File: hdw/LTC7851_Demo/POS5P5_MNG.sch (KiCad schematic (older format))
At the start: 8 parts

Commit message: Added component values for all phase 1 components
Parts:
- removed C?: 100uF, symbol LED_Display_Local_Library:CP_Tant_Custom
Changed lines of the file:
@@
 $Descr A 11000 8500
 encoding utf-8
-Sheet 8 15
+Sheet 8 14
 Title ""
 Date ""
@@
 Comment4 ""
 $EndDescr
-$Comp
-L LED_Display_Local_Library:CP_Tant_Custom C?
-U 1 1 5BBB1259
-P 7040 3820
-AR Path="/5BB86F23/5BBB1259" Ref="C?"  Part="1"
-AR Path="/5BB9CE4B/5BBB1259" Ref="C?"  Part="1"
-F 0 "C?" H 7065 3920 50  0000 L CNN
-F 1 "100uF" H 7065 3720 50  0000 L CNN
-F 2 "" H 7078 3670 50  0001 C CNN
-F 3 "" H 7065 3920 50  0001 C CNN
-F 4 "718-1102-1-ND" H 7040 3820 50  0001 C CNN "Digi-Key PN"
-F 5 "7343" H 6890 3920 50  0000 R CNN "display_footprint"
-F 6 "16V" H 6890 3820 50  0000 R CNN "Voltage"
-F 7 "10%" H 6890 3720 50  0000 R CNN "Tolerance"
-	1    7040 3820
-	1    0    0    -1
-$EndComp
 Wire Wire Line
 	3800 3510 3800 3590

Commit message: Duplicated master phase, added status LEDs and a few test points
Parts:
- removed C?: C, symbol Custom_Library:C_Custom
- removed C?: 10uF, symbol Custom_Library:C_Custom
- removed R?: R, symbol Custom_Library:R_Custom
- added C?: 100uF, symbol Custom_Library:CP_Tant_Custom
- added C?: 0.1uF, symbol Custom_Library:C_Custom
- added C?: 10uF, symbol Custom_Library:CP_Tant_Custom
- added R?: 680, symbol Custom_Library:R_Custom
- R?: value R -> 200; Tolerance Tol -> 1%; Wattage W -> 1/10W; display_footprint Foot -> 0603
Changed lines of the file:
@@
-$Comp
-L Custom_Library:C_Custom C?
-U 1 1 5BBB0B35
-P 3800 3820
-F 0 "C?" H 3825 3920 50  0000 L CNN
-F 1 "10uF" H 3825 3720 50  0000 L CNN
-F 2 "" H 3838 3670 50  0001 C CNN
-F 3 "" H 3825 3920 50  0001 C CNN
-F 4 "Foot" H 3650 3920 50  0000 R CNN "display_footprint"
-F 5 "V" H 3650 3820 50  0000 R CNN "Voltage"
-F 6 "Er" H 3650 3720 50  0000 R CNN "Dielectric"
-F 7 "PN" H 4225 4320 60  0001 C CNN "Digi-Key PN"
-	1    3800 3820
-	1    0    0    -1
-$EndComp
 $Comp
 L Custom_Library:C_Custom C?
@@
 $EndComp
 $Comp
-L Custom_Library:C_Custom C?
-U 1 1 5BBB004E
-P 5130 4280
-F 0 "C?" H 5155 4380 50  0000 L CNN
-F 1 "C" H 5155 4180 50  0000 L CNN
-F 2 "" H 5168 4130 50  0001 C CNN
-F 3 "" H 5155 4380 50  0001 C CNN
-F 4 "Foot" H 4980 4380 50  0000 R CNN "display_footprint"
-F 5 "V" H 4980 4280 50  0000 R CNN "Voltage"
-F 6 "Er" H 4980 4180 50  0000 R CNN "Dielectric"
-F 7 "PN" H 5555 4780 60  0001 C CNN "Digi-Key PN"
-	1    5130 4280
-	1    0    0    -1
-$EndComp
-$Comp
 L power:GND #PWR?
 U 1 1 5BBAFFEC
@@
 $Comp
 L Custom_Library:R_Custom R?
-U 1 1 5BBAFF2B
-P 5770 4280
-AR Path="/5BB86F29/5BBAFF2B" Ref="R?"  Part="1"
-AR Path="/5BB9CE4B/5BBAFF2B" Ref="R?"  Part="1"
-F 0 "R?" H 5670 4280 50  0000 R CNN
-F 1 "R" V 5770 4280 50  0000 C CNN
-F 2 "" H 5770 4280 50  0001 C CNN
-F 3 "" H 5770 4280 50  0001 C CNN
-F 4 "PN" H 6070 4680 60  0001 C CNN "Digi-Key PN"
-F 5 "Foot" H 5870 4360 50  0000 L CNN "display_footprint"
-F 6 "Tol" H 5870 4280 50  0000 L CNN "Tolerance"
-F 7 "W" H 5870 4200 50  0000 L CNN "Wattage"
-	1    5770 4280
-	-1   0    0    -1
-$EndComp
-$Comp
-L Custom_Library:R_Custom R?
 U 1 1 5BBAFF04
 P 5770 3820
@@
 AR Path="/5BB9CE4B/5BBAFF04" Ref="R?"  Part="1"
 F 0 "R?" H 5670 3820 50  0000 R CNN
-F 1 "R" V 5770 3820 50  0000 C CNN
+F 1 "200" V 5770 3820 50  0000 C CNN
 F 2 "" H 5770 3820 50  0001 C CNN
 F 3 "" H 5770 3820 50  0001 C CNN
 F 4 "PN" H 6070 4220 60  0001 C CNN "Digi-Key PN"
-F 5 "Foot" H 5870 3900 50  0000 L CNN "display_footprint"
-F 6 "Tol" H 5870 3820 50  0000 L CNN "Tolerance"
-F 7 "W" H 5870 3740 50  0000 L CNN "Wattage"
+F 5 "0603" H 5870 3900 50  0000 L CNN "display_footprint"
+F 6 "1%" H 5870 3820 50  0000 L CNN "Tolerance"
+F 7 "1/10W" H 5870 3740 50  0000 L CNN "Wattage"
 	1    5770 3820
 	-1   0    0    -1
@@
 	1    0    0    -1
 $EndComp
+$Comp
+L Custom_Library:CP_Tant_Custom C?
+U 1 1 5BD4FFF4
+P 7040 3820
+AR Path="/5BB86F29/5BD4FFF4" Ref="C?"  Part="1"
+AR Path="/5BB86F2C/5BD4FFF4" Ref="C?"  Part="1"
+AR Path="/5BB86F2F/5BD4FFF4" Ref="C?"  Part="1"
+AR Path="/5BB9CE4B/5BD4FFF4" Ref="C?"  Part="1"
+F 0 "C?" H 7065 3920 50  0000 L CNN
+F 1 "100uF" H 7065 3720 50  0000 L CNN
+F 2 "" H 7078 3670 50  0001 C CNN
+F 3 "" H 7065 3920 50  0001 C CNN
+F 4 "478-9994-1-ND" H 7040 3820 50  0001 C CNN "Digi-Key PN"
+F 5 "3528" H 6890 3920 50  0000 R CNN "display_footprint"
+F 6 "6.3V" H 6890 3820 50  0000 R CNN "Voltage"
+F 7 "20%" H 6890 3720 50  0000 R CNN "Tolerance"
+	1    7040 3820
+	1    0    0    -1
+$EndComp
+$Comp
+L Custom_Library:R_Custom R?
+U 1 1 5BD50813
+P 5770 4280
+AR Path="/5BB86F29/5BD50813" Ref="R?"  Part="1"
+AR Path="/5BB9CE4B/5BD50813" Ref="R?"  Part="1"
+F 0 "R?" H 5670 4280 50  0000 R CNN
+F 1 "680" V 5770 4280 50  0000 C CNN
+F 2 "" H 5770 4280 50  0001 C CNN
+F 3 "" H 5770 4280 50  0001 C CNN
+F 4 "PN" H 6070 4680 60  0001 C CNN "Digi-Key PN"
+F 5 "0603" H 5870 4360 50  0000 L CNN "display_footprint"
+F 6 "1%" H 5870 4280 50  0000 L CNN "Tolerance"
+F 7 "1/10W" H 5870 4200 50  0000 L CNN "Wattage"
+	1    5770 4280
+	-1   0    0    -1
+$EndComp
+$Comp
+L Custom_Library:C_Custom C?
+U 1 1 5BD51214
+P 5130 4280
+F 0 "C?" H 5155 4380 50  0000 L CNN
+F 1 "0.1uF" H 5155 4180 50  0000 L CNN
+F 2 "" H 5168 4130 50  0001 C CNN
+F 3 "" H 5155 4380 50  0001 C CNN
+F 4 "0603" H 4980 4380 50  0000 R CNN "display_footprint"
+F 5 "50V" H 4980 4280 50  0000 R CNN "Voltage"
+F 6 "X7R" H 4980 4180 50  0000 R CNN "Dielectric"
+F 7 "PN" H 5555 4780 60  0001 C CNN "Digi-Key PN"
+	1    5130 4280
+	1    0    0    -1
+$EndComp
+$Comp
+L Custom_Library:CP_Tant_Custom C?
+U 1 1 5BD5196E
+P 3800 3820
+AR Path="/5BB86F29/5BD5196E" Ref="C?"  Part="1"
+AR Path="/5BB86F2C/5BD5196E" Ref="C?"  Part="1"
+AR Path="/5BB86F2F/5BD5196E" Ref="C?"  Part="1"
+AR Path="/5BB9CE4B/5BD5196E" Ref="C?"  Part="1"
+F 0 "C?" H 3825 3920 50  0000 L CNN
+F 1 "10uF" H 3825 3720 50  0000 L CNN
+F 2 "" H 3838 3670 50  0001 C CNN
+F 3 "" H 3825 3920 50  0001 C CNN
+F 4 "399-5034-1-ND" H 3800 3820 50  0001 C CNN "Digi-Key PN"
+F 5 "3528" H 3650 3920 50  0000 R CNN "display_footprint"
+F 6 "16V" H 3650 3820 50  0000 R CNN "Voltage"
+F 7 "10%" H 3650 3720 50  0000 R CNN "Tolerance"
+	1    3800 3820
+	1    0    0    -1
+$EndComp

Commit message: Annotated schematic
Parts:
- added TP801: TP, symbol Custom_Library:TP
- gave numbers to parts that had none: 8
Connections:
- wire segments 17 -> 19
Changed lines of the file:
@@
 	3800 3510 3800 3590
 $Comp
-L power:+12V #PWR?
+L power:+12V #PWR0801
 U 1 1 5BBB0D98
 P 3800 3510
-F 0 "#PWR?" H 3800 3360 50  0001 C CNN
+F 0 "#PWR0801" H 3800 3360 50  0001 C CNN
 F 1 "+12V" H 3800 3650 50  0000 C CNN
 F 2 "" H 3800 3510 50  0001 C CNN
@@
 	3800 3670 3800 3590
 $Comp
-L power:GND #PWR?
+L power:GND #PWR0802
 U 1 1 5BBB0B8E
 P 3800 3970
-F 0 "#PWR?" H 3800 3720 50  0001 C CNN
+F 0 "#PWR0802" H 3800 3720 50  0001 C CNN
 F 1 "GND" H 3800 3820 50  0000 C CNN
 F 2 "" H 3800 3970 50  0001 C CNN
@@
 $EndComp
 $Comp
-L power:GND #PWR?
+L power:GND #PWR0803
 U 1 1 5BBB0B63
 P 4460 3970
-F 0 "#PWR?" H 4460 3720 50  0001 C CNN
+F 0 "#PWR0803" H 4460 3720 50  0001 C CNN
 F 1 "GND" H 4460 3820 50  0000 C CNN
 F 2 "" H 4460 3970 50  0001 C CNN
@@
 $EndComp
 $Comp
-L Custom_Library:C_Custom C?
+L Custom_Library:C_Custom C802
 U 1 1 5BBB0AFB
 P 4460 3820
-F 0 "C?" H 4485 3920 50  0000 L CNN
+F 0 "C802" H 4485 3920 50  0000 L CNN
 F 1 "0.1uF" H 4485 3720 50  0000 L CNN
 F 2 "" H 4498 3670 50  0001 C CNN
@@
 	7040 3510 7040 3590
 $Comp
-L Custom_Library:+5.5V_MNG #PWR?
+L Custom_Library:+5.5V_MNG #PWR0807
 U 1 1 5BBB0807
 P 7040 3510
-F 0 "#PWR?" H 7040 3360 50  0001 C CNN
+F 0 "#PWR0807" H 7040 3360 50  0001 C CNN
 F 1 "+5.5V_MNG" H 7040 3650 50  0000 C CNN
 F 2 "" H 7040 3510 50  0001 C CNN
@@
 	7040 3670 7040 3590
 $Comp
-L power:GND #PWR?
+L power:GND #PWR0808
 U 1 1 5BBB04B3
 P 7040 3970
-F 0 "#PWR?" H 7040 3720 50  0001 C CNN
+F 0 "#PWR0808" H 7040 3720 50  0001 C CNN
 F 1 "GND" H 7040 3820 50  0000 C CNN
 F 2 "" H 7040 3970 50  0001 C CNN
@@
 	6430 3670 6430 3590
 $Comp
-L power:GND #PWR?
+L power:GND #PWR0806
 U 1 1 5BBB0393
 P 6430 3970
-F 0 "#PWR?" H 6430 3720 50  0001 C CNN
+F 0 "#PWR0806" H 6430 3720 50  0001 C CNN
 F 1 "GND" H 6430 3820 50  0000 C CNN
 F 2 "" H 6430 3970 50  0001 C CNN
@@
 $EndComp
 $Comp
-L Custom_Library:C_Custom C?
+L Custom_Library:C_Custom C804
 U 1 1 5BBB0328
 P 6430 3820
-F 0 "C?" H 6455 3920 50  0000 L CNN
+F 0 "C804" H 6455 3920 50  0000 L CNN
 F 1 "0.1uF" H 6455 3720 50  0000 L CNN
 F 2 "" H 6468 3670 50  0001 C CNN
@@
 	5130 4130 5130 4040
 $Comp
-L power:GND #PWR?
+L power:GND #PWR0804
 U 1 1 5BBB0089
 P 5130 4430
-F 0 "#PWR?" H 5130 4180 50  0001 C CNN
+F 0 "#PWR0804" H 5130 4180 50  0001 C CNN
 F 1 "GND" H 5130 4280 50  0000 C CNN
 F 2 "" H 5130 4430 50  0001 C CNN
@@
 $EndComp
 $Comp
-L power:GND #PWR?
+L power:GND #PWR0805
 U 1 1 5BBAFFEC
 P 5770 4430
-F 0 "#PWR?" H 5770 4180 50  0001 C CNN
+F 0 "#PWR0805" H 5770 4180 50  0001 C CNN
 F 1 "GND" H 5770 4280 50  0000 C CNN
 F 2 "" H 5770 4430 50  0001 C CNN
@@
 P 5770 3820
 AR Path="/5BB86F29/5BBAFF04" Ref="R?"  Part="1"
-AR Path="/5BB9CE4B/5BBAFF04" Ref="R?"  Part="1"
-F 0 "R?" H 5670 3820 50  0000 R CNN
+AR Path="/5BB9CE4B/5BBAFF04" Ref="R801"  Part="1"
+F 0 "R801" H 5670 3820 50  0000 R CNN
 F 1 "200" V 5770 3820 50  0000 C CNN
 F 2 "" H 5770 3820 50  0001 C CNN
@@
 $EndComp
 $Comp
-L Regulator_Linear:LM1117-ADJ U?
+L Regulator_Linear:LM1117-ADJ U801
 U 1 1 5BBA7A89
 P 5130 3590
-F 0 "U?" H 4980 3715 50  0000 C CNN
+F 0 "U801" H 4980 3715 50  0000 C CNN
 F 1 "LM1117-ADJ" H 5130 3715 50  0000 L CNN
 F 2 "" H 5130 3590 50  0001 C CNN
@@
 AR Path="/5BB86F2C/5BD4FFF4" Ref="C?"  Part="1"
 AR Path="/5BB86F2F/5BD4FFF4" Ref="C?"  Part="1"
-AR Path="/5BB9CE4B/5BD4FFF4" Ref="C?"  Part="1"
-F 0 "C?" H 7065 3920 50  0000 L CNN
+AR Path="/5BB9CE4B/5BD4FFF4" Ref="C805"  Part="1"
+F 0 "C805" H 7065 3920 50  0000 L CNN
 F 1 "100uF" H 7065 3720 50  0000 L CNN
 F 2 "" H 7078 3670 50  0001 C CNN
@@
 P 5770 4280
 AR Path="/5BB86F29/5BD50813" Ref="R?"  Part="1"
-AR Path="/5BB9CE4B/5BD50813" Ref="R?"  Part="1"
-F 0 "R?" H 5670 4280 50  0000 R CNN
+AR Path="/5BB9CE4B/5BD50813" Ref="R802"  Part="1"
+F 0 "R802" H 5670 4280 50  0000 R CNN
 F 1 "680" V 5770 4280 50  0000 C CNN
 F 2 "" H 5770 4280 50  0001 C CNN
@@
 $EndComp
 $Comp
-L Custom_Library:C_Custom C?
+L Custom_Library:C_Custom C803
 U 1 1 5BD51214
 P 5130 4280
-F 0 "C?" H 5155 4380 50  0000 L CNN
+F 0 "C803" H 5155 4380 50  0000 L CNN
 F 1 "0.1uF" H 5155 4180 50  0000 L CNN
 F 2 "" H 5168 4130 50  0001 C CNN
@@
 AR Path="/5BB86F2C/5BD5196E" Ref="C?"  Part="1"
 AR Path="/5BB86F2F/5BD5196E" Ref="C?"  Part="1"
-AR Path="/5BB9CE4B/5BD5196E" Ref="C?"  Part="1"
-F 0 "C?" H 3825 3920 50  0000 L CNN
+AR Path="/5BB9CE4B/5BD5196E" Ref="C801"  Part="1"
+F 0 "C801" H 3825 3920 50  0000 L CNN
 F 1 "10uF" H 3825 3720 50  0000 L CNN
 F 2 "" H 3838 3670 50  0001 C CNN
@@
 	1    0    0    -1
 $EndComp
+$Comp
+L power:PWR_FLAG #FLG0801
+U 1 1 5BC40B21
+P 5770 3510
+F 0 "#FLG0801" H 5770 3585 50  0001 C CNN
+F 1 "PWR_FLAG" H 5770 3660 50  0000 C CNN
+F 2 "" H 5770 3510 50  0001 C CNN
+F 3 "~" H 5770 3510 50  0001 C CNN
+	1    5770 3510
+	1    0    0    -1
+$EndComp
+Wire Wire Line
+	5770 3510 5770 3590
+$Comp
+L Custom_Library:TP TP801
+U 1 1 5BC40C98
+P 6430 3510
+F 0 "TP801" H 6430 3660 50  0000 C CNN
+F 1 "TP" H 6430 3660 50  0001 C CNN
+F 2 "" H 6430 3510 60  0000 C CNN
+F 3 "" H 6430 3510 60  0000 C CNN
+	1    6430 3510
+	1    0    0    -1
+$EndComp
+Wire Wire Line
+	6430 3510 6430 3590
 $EndSCHEMATC

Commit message: Cleaned up for ERC
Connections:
- wire segments 19 -> 18
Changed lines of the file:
@@
 $EndComp
-$Comp
-L power:PWR_FLAG #FLG0801
-U 1 1 5BC40B21
-P 5770 3510
-F 0 "#FLG0801" H 5770 3585 50  0001 C CNN
-F 1 "PWR_FLAG" H 5770 3660 50  0000 C CNN
-F 2 "" H 5770 3510 50  0001 C CNN
-F 3 "~" H 5770 3510 50  0001 C CNN
-	1    5770 3510
-	1    0    0    -1
-$EndComp
-Wire Wire Line
-	5770 3510 5770 3590
 $Comp
 L Custom_Library:TP TP801

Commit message: Added Digi-Key part numbers for all parts
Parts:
- C802, C803, C804: Digi-Key PN PN -> 490-4779-1-ND
- R801: Digi-Key PN PN -> MCT0603-200-CFCT-ND
- R802: Digi-Key PN PN -> P680HCT-ND
- U801: Digi-Key PN (none) -> LM1117IMPX-ADJ/NOPBCT-ND
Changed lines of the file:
@@
 F 5 "50V" H 4310 3820 50  0000 R CNN "Voltage"
 F 6 "X7R" H 4310 3720 50  0000 R CNN "Dielectric"
-F 7 "PN" H 4885 4320 60  0001 C CNN "Digi-Key PN"
+F 7 "490-4779-1-ND" H 4885 4320 60  0001 C CNN "Digi-Key PN"
 	1    4460 3820
 	1    0    0    -1
@@
 F 5 "50V" H 6280 3820 50  0000 R CNN "Voltage"
 F 6 "X7R" H 6280 3720 50  0000 R CNN "Dielectric"
-F 7 "PN" H 6855 4320 60  0001 C CNN "Digi-Key PN"
+F 7 "490-4779-1-ND" H 6855 4320 60  0001 C CNN "Digi-Key PN"
 	1    6430 3820
 	1    0    0    -1
@@
 F 2 "" H 5770 3820 50  0001 C CNN
 F 3 "" H 5770 3820 50  0001 C CNN
-F 4 "PN" H 6070 4220 60  0001 C CNN "Digi-Key PN"
+F 4 "MCT0603-200-CFCT-ND" H 6070 4220 60  0001 C CNN "Digi-Key PN"
 F 5 "0603" H 5870 3900 50  0000 L CNN "display_footprint"
 F 6 "1%" H 5870 3820 50  0000 L CNN "Tolerance"
@@
 F 2 "" H 5130 3590 50  0001 C CNN
 F 3 "http://www.ti.com/lit/ds/symlink/lm1117.pdf" H 5130 3590 50  0001 C CNN
+F 4 "LM1117IMPX-ADJ/NOPBCT-ND" H 0   0   50  0001 C CNN "Digi-Key PN"
 	1    5130 3590
 	1    0    0    -1
@@
 F 2 "" H 5770 4280 50  0001 C CNN
 F 3 "" H 5770 4280 50  0001 C CNN
-F 4 "PN" H 6070 4680 60  0001 C CNN "Digi-Key PN"
+F 4 "P680HCT-ND" H 6070 4680 60  0001 C CNN "Digi-Key PN"
 F 5 "0603" H 5870 4360 50  0000 L CNN "display_footprint"
 F 6 "1%" H 5870 4280 50  0000 L CNN "Tolerance"
@@
 F 5 "50V" H 4980 4280 50  0000 R CNN "Voltage"
 F 6 "X7R" H 4980 4180 50  0000 R CNN "Dielectric"
-F 7 "PN" H 5555 4780 60  0001 C CNN "Digi-Key PN"
+F 7 "490-4779-1-ND" H 5555 4780 60  0001 C CNN "Digi-Key PN"
 	1    5130 4280
 	1    0    0    -1

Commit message: Assigned footprints
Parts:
- C801, C805: footprint (none) -> Capacitors_Tantalum_SMD:CP_Tantalum_Case-B_EIA-3528-21_Reflow
- C802, C803, C804: footprint (none) -> Capacitors_SMD:C_0603
- R801, R802: footprint (none) -> Resistors_SMD:R_0603
- TP801: footprint (none) -> Measurement_Points:Measurement_Point_Round-SMD-Pad_Small
- U801: footprint (none) -> TO_SOT_Packages_SMD:SOT-223-3_TabPin2
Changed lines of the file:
@@
 F 0 "C802" H 4485 3920 50  0000 L CNN
 F 1 "0.1uF" H 4485 3720 50  0000 L CNN
-F 2 "" H 4498 3670 50  0001 C CNN
+F 2 "Capacitors_SMD:C_0603" H 4498 3670 50  0001 C CNN
 F 3 "" H 4485 3920 50  0001 C CNN
 F 4 "0603" H 4310 3920 50  0000 R CNN "display_footprint"
@@
 F 0 "C804" H 6455 3920 50  0000 L CNN
 F 1 "0.1uF" H 6455 3720 50  0000 L CNN
-F 2 "" H 6468 3670 50  0001 C CNN
+F 2 "Capacitors_SMD:C_0603" H 6468 3670 50  0001 C CNN
 F 3 "" H 6455 3920 50  0001 C CNN
 F 4 "0603" H 6280 3920 50  0000 R CNN "display_footprint"
@@
 F 0 "R801" H 5670 3820 50  0000 R CNN
 F 1 "200" V 5770 3820 50  0000 C CNN
-F 2 "" H 5770 3820 50  0001 C CNN
+F 2 "Resistors_SMD:R_0603" H 5770 3820 50  0001 C CNN
 F 3 "" H 5770 3820 50  0001 C CNN
 F 4 "MCT0603-200-CFCT-ND" H 6070 4220 60  0001 C CNN "Digi-Key PN"
@@
 F 0 "U801" H 4980 3715 50  0000 C CNN
 F 1 "LM1117-ADJ" H 5130 3715 50  0000 L CNN
-F 2 "" H 5130 3590 50  0001 C CNN
+F 2 "TO_SOT_Packages_SMD:SOT-223-3_TabPin2" H 5130 3590 50  0001 C CNN
 F 3 "http://www.ti.com/lit/ds/symlink/lm1117.pdf" H 5130 3590 50  0001 C CNN
 F 4 "LM1117IMPX-ADJ/NOPBCT-ND" H 0   0   50  0001 C CNN "Digi-Key PN"
@@
 F 0 "C805" H 7065 3920 50  0000 L CNN
 F 1 "100uF" H 7065 3720 50  0000 L CNN
-F 2 "" H 7078 3670 50  0001 C CNN
+F 2 "Capacitors_Tantalum_SMD:CP_Tantalum_Case-B_EIA-3528-21_Reflow" H 7078 3670 50  0001 C CNN
 F 3 "" H 7065 3920 50  0001 C CNN
 F 4 "478-9994-1-ND" H 7040 3820 50  0001 C CNN "Digi-Key PN"
@@
 F 0 "R802" H 5670 4280 50  0000 R CNN
 F 1 "680" V 5770 4280 50  0000 C CNN
-F 2 "" H 5770 4280 50  0001 C CNN
+F 2 "Resistors_SMD:R_0603" H 5770 4280 50  0001 C CNN
 F 3 "" H 5770 4280 50  0001 C CNN
 F 4 "P680HCT-ND" H 6070 4680 60  0001 C CNN "Digi-Key PN"
@@
 F 0 "C803" H 5155 4380 50  0000 L CNN
 F 1 "0.1uF" H 5155 4180 50  0000 L CNN
-F 2 "" H 5168 4130 50  0001 C CNN
+F 2 "Capacitors_SMD:C_0603" H 5168 4130 50  0001 C CNN
 F 3 "" H 5155 4380 50  0001 C CNN
 F 4 "0603" H 4980 4380 50  0000 R CNN "display_footprint"
@@
 F 0 "C801" H 3825 3920 50  0000 L CNN
 F 1 "10uF" H 3825 3720 50  0000 L CNN
-F 2 "" H 3838 3670 50  0001 C CNN
+F 2 "Capacitors_Tantalum_SMD:CP_Tantalum_Case-B_EIA-3528-21_Reflow" H 3838 3670 50  0001 C CNN
 F 3 "" H 3825 3920 50  0001 C CNN
 F 4 "399-5034-1-ND" H 3800 3820 50  0001 C CNN "Digi-Key PN"
@@
 F 0 "TP801" H 6430 3660 50  0000 C CNN
 F 1 "TP" H 6430 3660 50  0001 C CNN
-F 2 "" H 6430 3510 60  0000 C CNN
+F 2 "Measurement_Points:Measurement_Point_Round-SMD-Pad_Small" H 6430 3510 60  0001 C CNN
 F 3 "" H 6430 3510 60  0000 C CNN
 	1    6430 3510

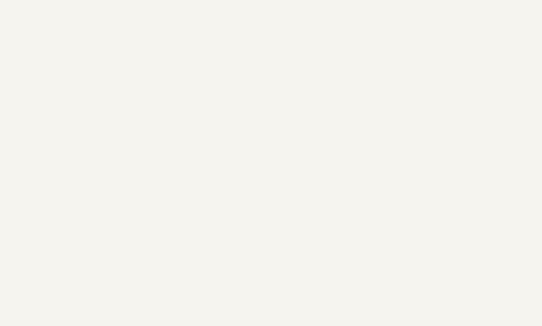
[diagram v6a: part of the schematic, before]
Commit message: Added page titles
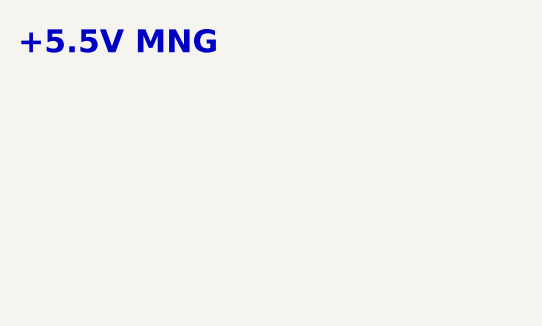
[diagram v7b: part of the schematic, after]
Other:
- note added: "+5.5V MNG"
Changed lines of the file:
@@
 Wire Wire Line
 	6430 3510 6430 3590
+Text Notes 540  690  0    100  ~ 20
++5.5V MNG
 $EndSCHEMATC
